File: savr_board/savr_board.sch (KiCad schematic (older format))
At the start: 7 parts, among them J1 SATA-7, J2 SATA-7, J3 SATA-7, J4 SATA-7, U1 XC7Z030-CLG485, U2 DDR3_256Mx16, U3 DDR3_256Mx16

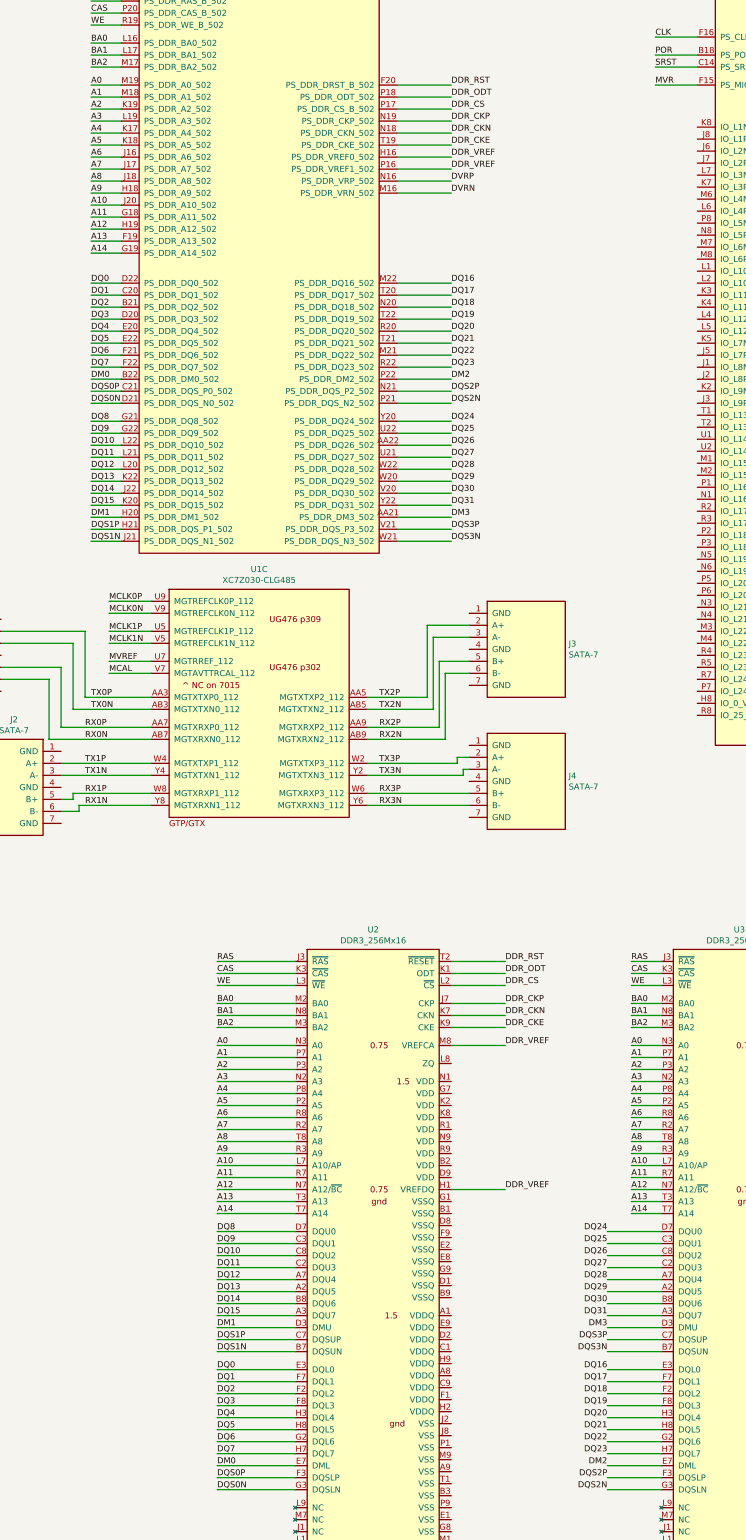
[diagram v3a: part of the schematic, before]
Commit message: Did a bunch of escape reshuffling and managed to route the DDR address and control lines. This probably won't work though since A10 and A12 have dual functionality that the CPU might use.
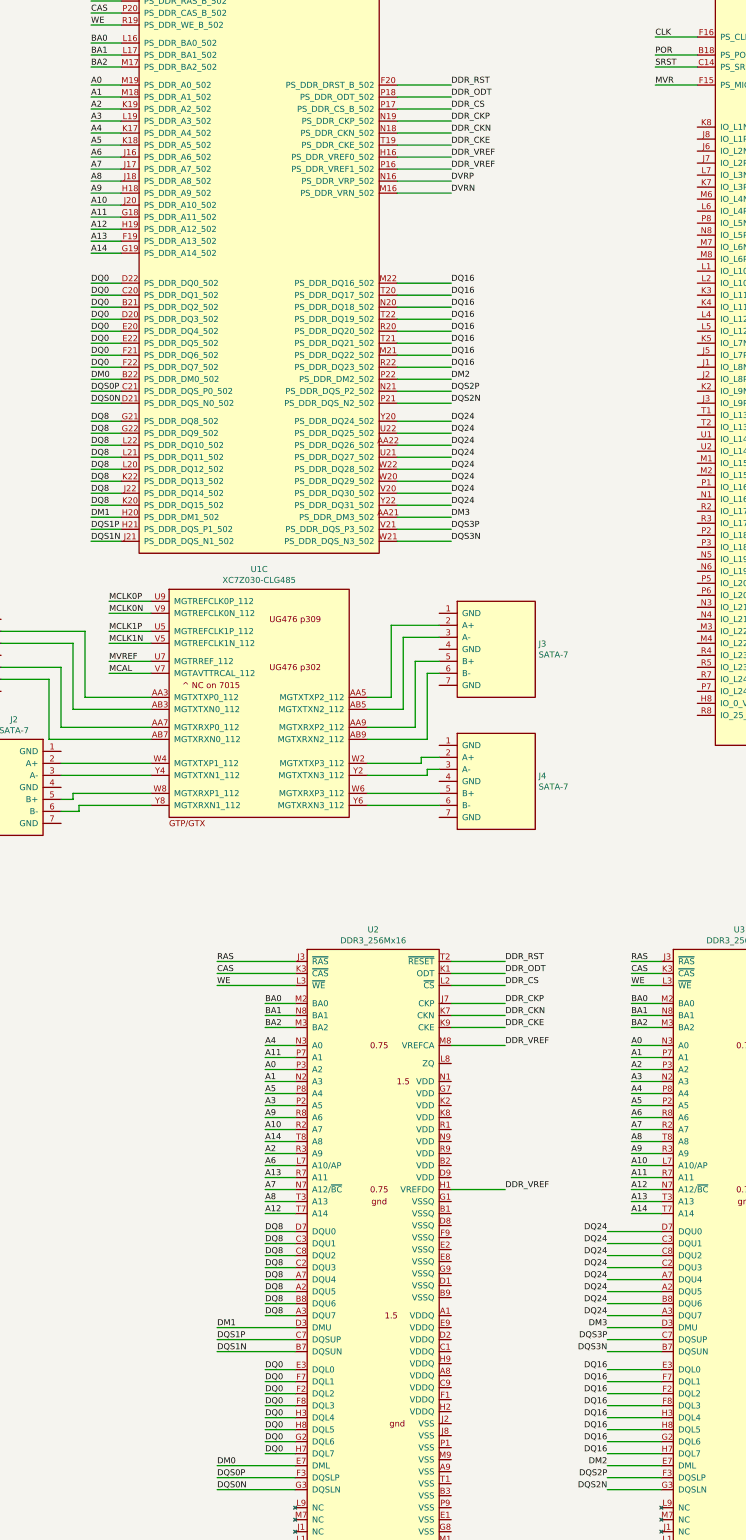
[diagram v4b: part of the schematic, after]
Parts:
- J1, J2, J3, J4: footprint savr_board:SATA-7-SMD-vert -> savr_board:SATA-7
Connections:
- net DQ1 is gone; now on net DQ0: U1.C20 (PS_DDR_DQ1_502), U2.F7 (DQL1)
- net DQ10 is gone; now on net DQ8: U1.L22 (PS_DDR_DQ10_502), U2.C8 (DQU2)
- net DQ11 is gone; now on net DQ8: U1.L21 (PS_DDR_DQ11_502), U2.C2 (DQU3)
- net DQ12 is gone; now on net DQ8: U1.L20 (PS_DDR_DQ12_502), U2.A7 (DQU4)
- net DQ13 is gone; now on net DQ8: U1.K22 (PS_DDR_DQ13_502), U2.A2 (DQU5)
- net DQ14 is gone; now on net DQ8: U1.J22 (PS_DDR_DQ14_502), U2.B8 (DQU6)
- net DQ15 is gone; now on net DQ8: U1.K20 (PS_DDR_DQ15_502), U2.A3 (DQU7)
- net DQ17 is gone; now on net DQ16: U1.T20 (PS_DDR_DQ17_502), U3.F7 (DQL1)
- net DQ18 is gone; now on net DQ16: U1.N20 (PS_DDR_DQ18_502), U3.F2 (DQL2)
- net DQ19 is gone; now on net DQ16: U1.T22 (PS_DDR_DQ19_502), U3.F8 (DQL3)
- net DQ2 is gone; now on net DQ0: U1.B21 (PS_DDR_DQ2_502), U2.F2 (DQL2)
- net DQ20 is gone; now on net DQ16: U1.R20 (PS_DDR_DQ20_502), U3.H3 (DQL4)
- net DQ21 is gone; now on net DQ16: U1.T21 (PS_DDR_DQ21_502), U3.H8 (DQL5)
- net DQ22 is gone; now on net DQ16: U1.M21 (PS_DDR_DQ22_502), U3.G2 (DQL6)
- net DQ23 is gone; now on net DQ16: U1.R22 (PS_DDR_DQ23_502), U3.H7 (DQL7)
- net DQ25 is gone; now on net DQ24: U1.U22 (PS_DDR_DQ25_502), U3.C3 (DQU1)
- net DQ26 is gone; now on net DQ24: U1.AA22 (PS_DDR_DQ26_502), U3.C8 (DQU2)
- net DQ27 is gone; now on net DQ24: U1.U21 (PS_DDR_DQ27_502), U3.C2 (DQU3)
- net DQ28 is gone; now on net DQ24: U1.W22 (PS_DDR_DQ28_502), U3.A7 (DQU4)
- net DQ29 is gone; now on net DQ24: U1.W20 (PS_DDR_DQ29_502), U3.A2 (DQU5)
- net DQ3 is gone; now on net DQ0: U1.D20 (PS_DDR_DQ3_502), U2.F8 (DQL3)
- net DQ30 is gone; now on net DQ24: U1.V20 (PS_DDR_DQ30_502), U3.B8 (DQU6)
- net DQ31 is gone; now on net DQ24: U1.Y22 (PS_DDR_DQ31_502), U3.A3 (DQU7)
- net DQ4 is gone; now on net DQ0: U1.E20 (PS_DDR_DQ4_502), U2.H3 (DQL4)
- net DQ5 is gone; now on net DQ0: U1.E22 (PS_DDR_DQ5_502), U2.H8 (DQL5)
- net DQ6 is gone; now on net DQ0: U1.F21 (PS_DDR_DQ6_502), U2.G2 (DQL6)
- net DQ7 is gone; now on net DQ0: U1.F22 (PS_DDR_DQ7_502), U2.H7 (DQL7)
- net DQ9 is gone; now on net DQ8: U1.G22 (PS_DDR_DQ9_502), U2.C3 (DQU1)
- net A0: now also U2.P3 (A2); no longer U2.N3 (A0)
- net A1: now also U2.N2 (A3); no longer U2.P7 (A1)
- net A10: now also U2.R2 (A7); no longer U2.L7 (A10/AP)
- net A11: now also U2.P7 (A1); no longer U2.R7 (A11)
- net A12: now also U2.T7 (A14); no longer U2.N7 (A12/~BC~)
- net A13: now also U2.R7 (A11); no longer U2.T3 (A13)
- net A14: now also U2.T8 (A8); no longer U2.T7 (A14)
- net A2: now also U2.R3 (A9); no longer U2.P3 (A2)
- net A3: now also U2.P2 (A5); no longer U2.N2 (A3)
- net A4: now also U2.N3 (A0); no longer U2.P8 (A4)
- net A5: now also U2.P8 (A4); no longer U2.P2 (A5)
- net A6: now also U2.L7 (A10/AP); no longer U2.R8 (A6)
- net A7: now also U2.N7 (A12/~BC~); no longer U2.R2 (A7)
- net A8: now also U2.T3 (A13); no longer U2.T8 (A8)
- net A9: now also U2.R8 (A6); no longer U2.R3 (A9)
- net RX0N: no longer names the net of J1.6 (B-), U1.AB7 (MGTXRXN0_112)
- net RX0P: no longer names the net of J1.5 (B+), U1.AA7 (MGTXRXP0_112)
- net RX1N: no longer names the net of J2.6 (B-), U1.Y8 (MGTXRXN1_112)
- net RX1P: no longer names the net of J2.5 (B+), U1.W8 (MGTXRXP1_112)
- net RX2N: no longer names the net of J3.6 (B-), U1.AB9 (MGTXRXN2_112)
- net RX2P: no longer names the net of J3.5 (B+), U1.AA9 (MGTXRXP2_112)
- net RX3N: no longer names the net of J4.6 (B-), U1.Y6 (MGTXRXN3_112)
- net RX3P: no longer names the net of J4.5 (B+), U1.W6 (MGTXRXP3_112)
- net TX0N: no longer names the net of J1.3 (A-), U1.AB3 (MGTXTXN0_112)
- net TX0P: no longer names the net of J1.2 (A+), U1.AA3 (MGTXTXP0_112)
- net TX1N: no longer names the net of J2.3 (A-), U1.Y4 (MGTXTXN1_112)
- net TX1P: no longer names the net of J2.2 (A+), U1.W4 (MGTXTXP1_112)
- net TX2N: no longer names the net of J3.3 (A-), U1.AB5 (MGTXTXN2_112)
- net TX2P: no longer names the net of J3.2 (A+), U1.AA5 (MGTXTXP2_112)
- net TX3N: no longer names the net of J4.3 (A-), U1.Y2 (MGTXTXN3_112)
- net TX3P: no longer names the net of J4.2 (A+), U1.W2 (MGTXTXP3_112)
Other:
- moved on the sheet: J3, J4

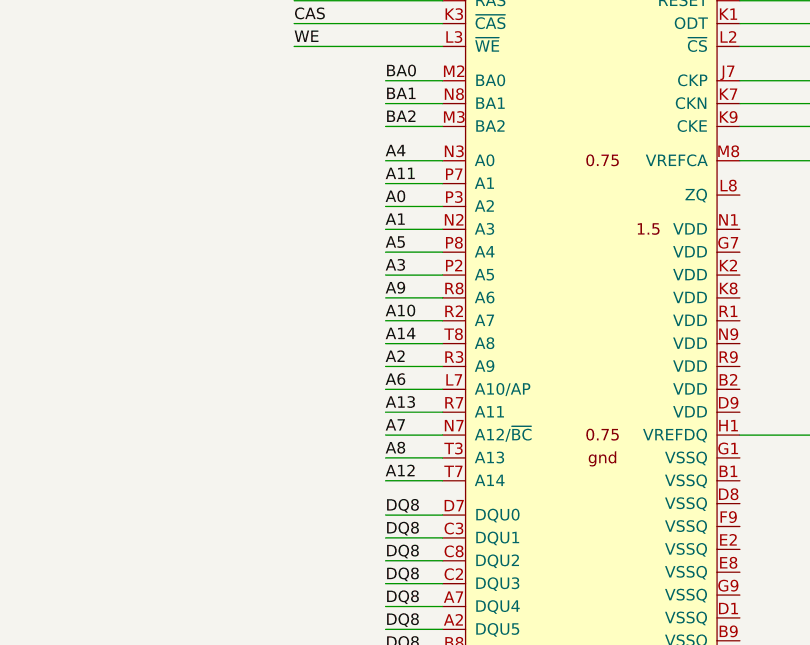
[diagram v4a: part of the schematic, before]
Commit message: Pin swaps to support A10/A12 being the same. I don't like this much since I had to put them on a different layer.
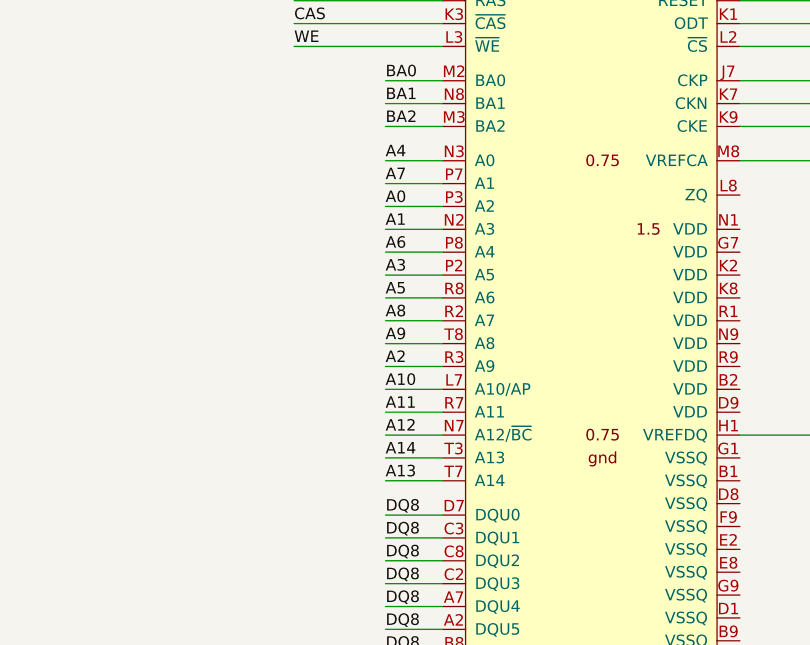
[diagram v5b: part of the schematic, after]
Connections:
- net A10: now also U2.L7 (A10/AP); no longer U2.R2 (A7)
- net A11: now also U2.R7 (A11); no longer U2.P7 (A1)
- net A12: now also U2.N7 (A12/~BC~); no longer U2.T7 (A14)
- net A13: now also U2.T7 (A14); no longer U2.R7 (A11)
- net A14: now also U2.T3 (A13); no longer U2.T8 (A8)
- net A5: now also U2.R8 (A6); no longer U2.P8 (A4)
- net A6: now also U2.P8 (A4); no longer U2.L7 (A10/AP)
- net A7: now also U2.P7 (A1); no longer U2.N7 (A12/~BC~)
- net A8: now also U2.R2 (A7); no longer U2.T3 (A13)
- net A9: now also U2.T8 (A8); no longer U2.R8 (A6)
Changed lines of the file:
@@
 	4400 9500 4150 9500
 Wire Wire Line
-	4400 9900 4150 9900
+	4400 10100 4150 10100
 Wire Wire Line
 	4400 10500 4150 10500
@@
 	4400 10700 4150 10700
 Wire Wire Line
-	4400 10800 4150 10800
+	4400 10200 4150 10200
 Wire Wire Line
-	4400 10100 4150 10100
+	4400 10300 4150 10300
 Wire Wire Line
-	4400 10200 4150 10200
+	4400 9900 4150 9900
+Wire Wire Line
+	4400 10600 4150 10600
 Wire Wire Line
 	4400 9600 4150 9600
 Wire Wire Line
-	4400 10900 4150 10900
-Wire Wire Line
-	4400 10600 4150 10600
-Wire Wire Line
-	4400 10300 4150 10300
+	4400 10800 4150 10800
 Text Label 4150 9700 0    50   ~ 0
 A0
@@
 Text Label 4150 9500 0    50   ~ 0
 A4
+Text Label 4150 10100 0    50   ~ 0
+A5
 Text Label 4150 9900 0    50   ~ 0
-A5
+A6
+Text Label 4150 9600 0    50   ~ 0
+A7
+Text Label 4150 10200 0    50   ~ 0
+A8
+Text Label 4150 10300 0    50   ~ 0
+A9
 Text Label 4150 10500 0    50   ~ 0
-A6
+A10
+Text Label 4150 10600 0    50   ~ 0
+A11
 Text Label 4150 10700 0    50   ~ 0
-A7
+A12
 Text Label 4150 10800 0    50   ~ 0
-A8
-Text Label 4150 10100 0    50   ~ 0
-A9
-Text Label 4150 10200 0    50   ~ 0
-A10
-Text Label 4150 9600 0    50   ~ 0
-A11
-Text Label 4150 10900 0    50   ~ 0
-A12
-Text Label 4150 10600 0    50   ~ 0
-A13
-Text Label 4150 10300 0    50   ~ 0
 A14
 Wire Wire Line
@@
 Text Label 7200 10900 0    50   ~ 0
 A14
+Text Label 4150 10900 0    50   ~ 0
+A13
+Wire Wire Line
+	4400 10900 4150 10900
 $EndSCHEMATC
